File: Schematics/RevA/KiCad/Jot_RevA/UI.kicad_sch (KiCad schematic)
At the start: 0 parts

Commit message: UI sheet: SW1 side button on BTN; buzzer BZ1 on +BATT with Q1 AO3400A low-side switch, R12 gate pull-down, D4 flyback, BUZZER_PWM
Co-Authored-By: Claude Opus 5.5 <noreply@anthropic.com>
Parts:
- added BZ1: MLT-5020, symbol Device:Buzzer
- added D4: 1N4148W, symbol Device:D
- added Q1: AO3400A, Package_TO_SOT_SMD:SOT-23, symbol Transistor_FET:AO3400A
- added R12: 100k, symbol Device:R
- added SW1: SW_Push, symbol Switch:SW_Push
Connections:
- new net: BZ1.2 (-), D4.2 (A), Q1.3 (D)
- new net +BATT: BZ1.1 (+), D4.1 (K)
- new net BTN: SW1.1
- new net BUZZER_PWM: Q1.1 (G), R12.1
- new net GND: Q1.2 (S), R12.2, SW1.2

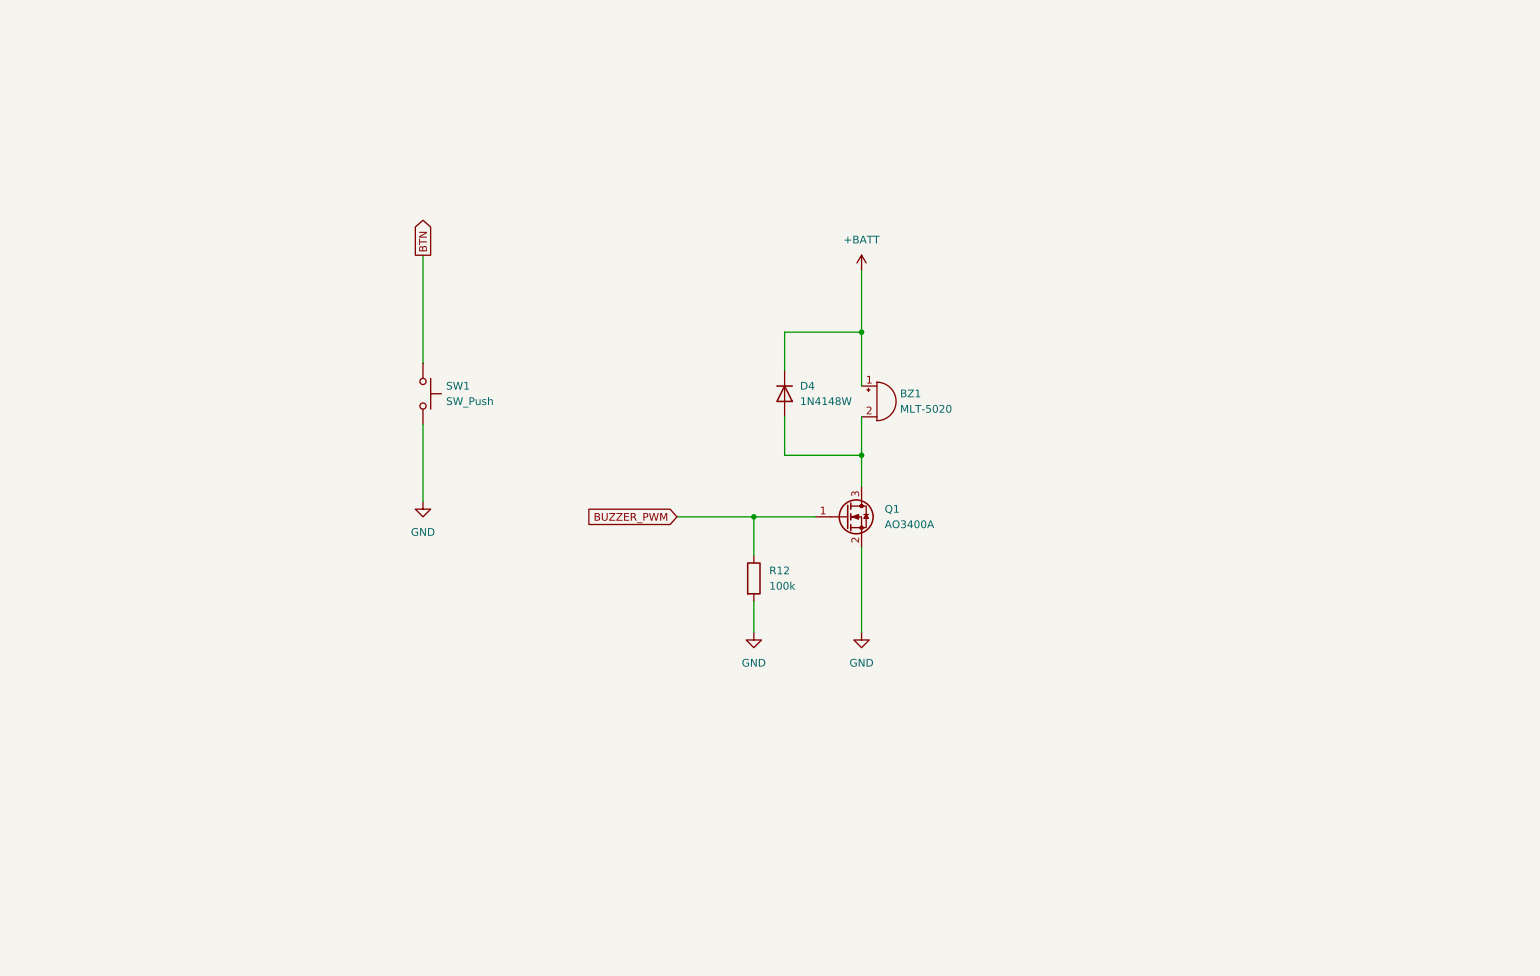
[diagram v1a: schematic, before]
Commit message: UI sheet: RGB LED D2 (common anode on +BATT) with R8 1k / R9 560 / R10 560 to Q3/Q4/Q5 low-side switches, R15-R17 gate pull-downs, LED_R/G/B labels
Co-Authored-By: Claude Opus 5.5 <noreply@anthropic.com>
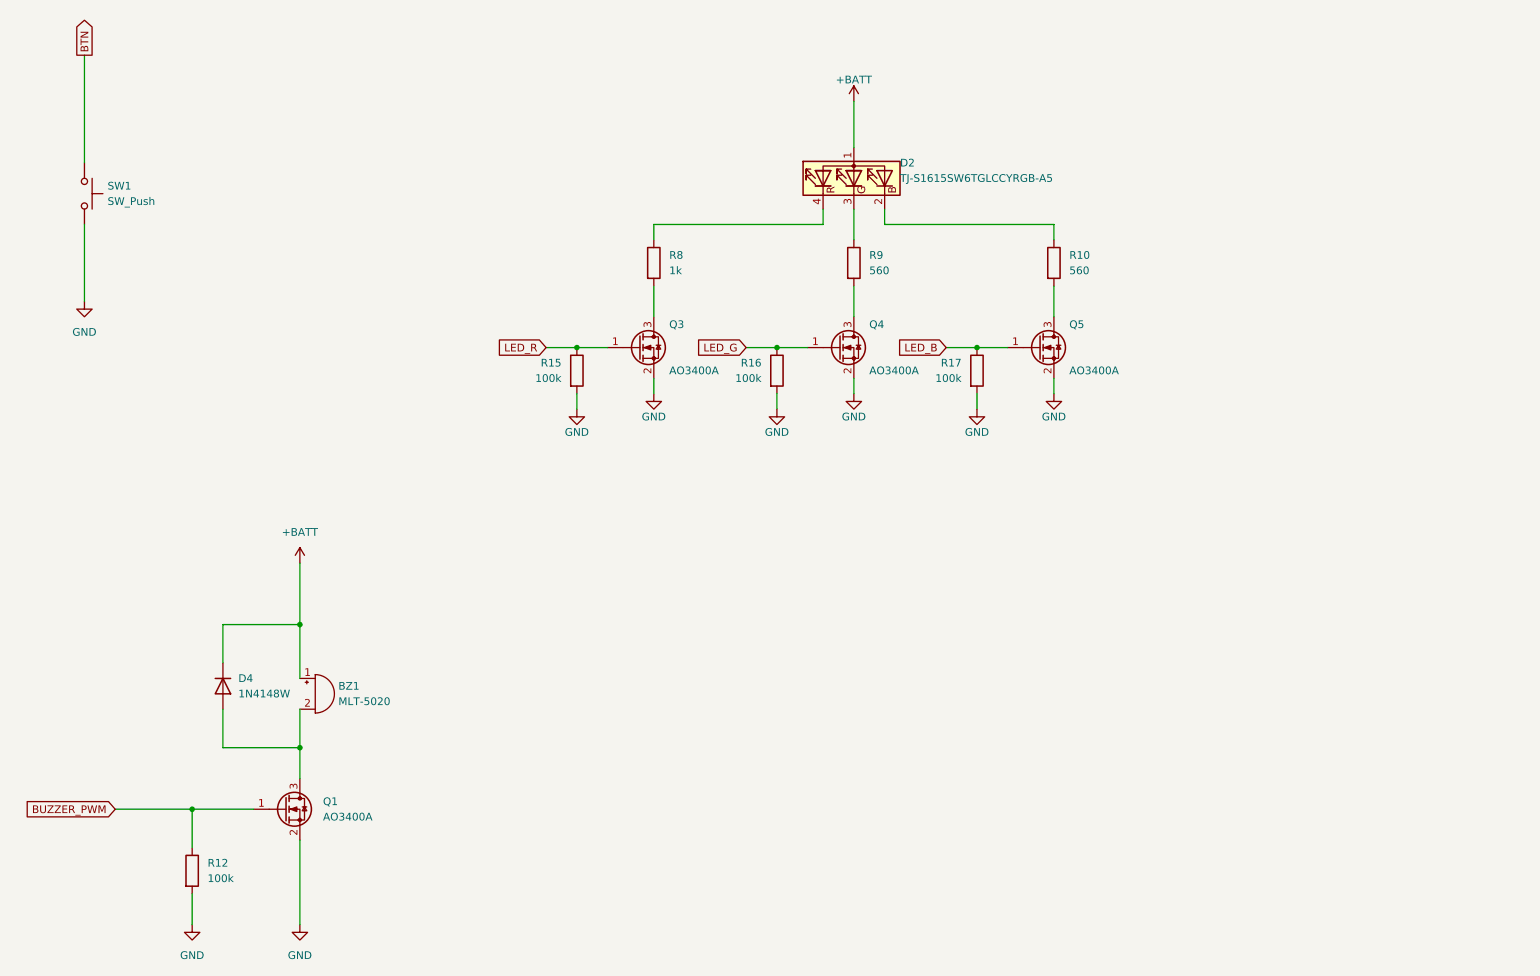
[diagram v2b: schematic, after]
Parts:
- added D2: TJ-S1615SW6TGLCCYRGB-A5, symbol Jot:TJ-S1615SW6TGLCCYRGB-A5
- added Q3, Q4, Q5: AO3400A, Package_TO_SOT_SMD:SOT-23, symbol Transistor_FET:AO3400A
- added R10, R9: 560, symbol Device:R
- added R15, R16, R17: 100k, symbol Device:R
- added R8: 1k, symbol Device:R
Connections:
- net +BATT: now also D2.1 (A)
- net GND: now also Q3.2 (S), Q4.2 (S), Q5.2 (S), R15.2, R16.2, R17.2
- new net: D2.2 (BK), R10.1
- new net: Q5.3 (D), R10.2
- new net: D2.3 (GK), R9.1
- new net: D2.4 (RK), R8.1
- new net: Q3.3 (D), R8.2
- new net: Q4.3 (D), R9.2
- new net LED_B: Q5.1 (G), R17.1
- new net LED_G: Q4.1 (G), R16.1
- new net LED_R: Q3.1 (G), R15.1
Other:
- moved on the sheet: BZ1, D4, Q1, R12, SW1

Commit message: Debug sheet: TP3-TP9 test pads for SWDIO, SWDCLK, nRESET, +3V3, GND, UART_TX, UART_RX; UI sheet re-laid out (nets unchanged)
Co-Authored-By: Claude Opus 5.5 <noreply@anthropic.com>
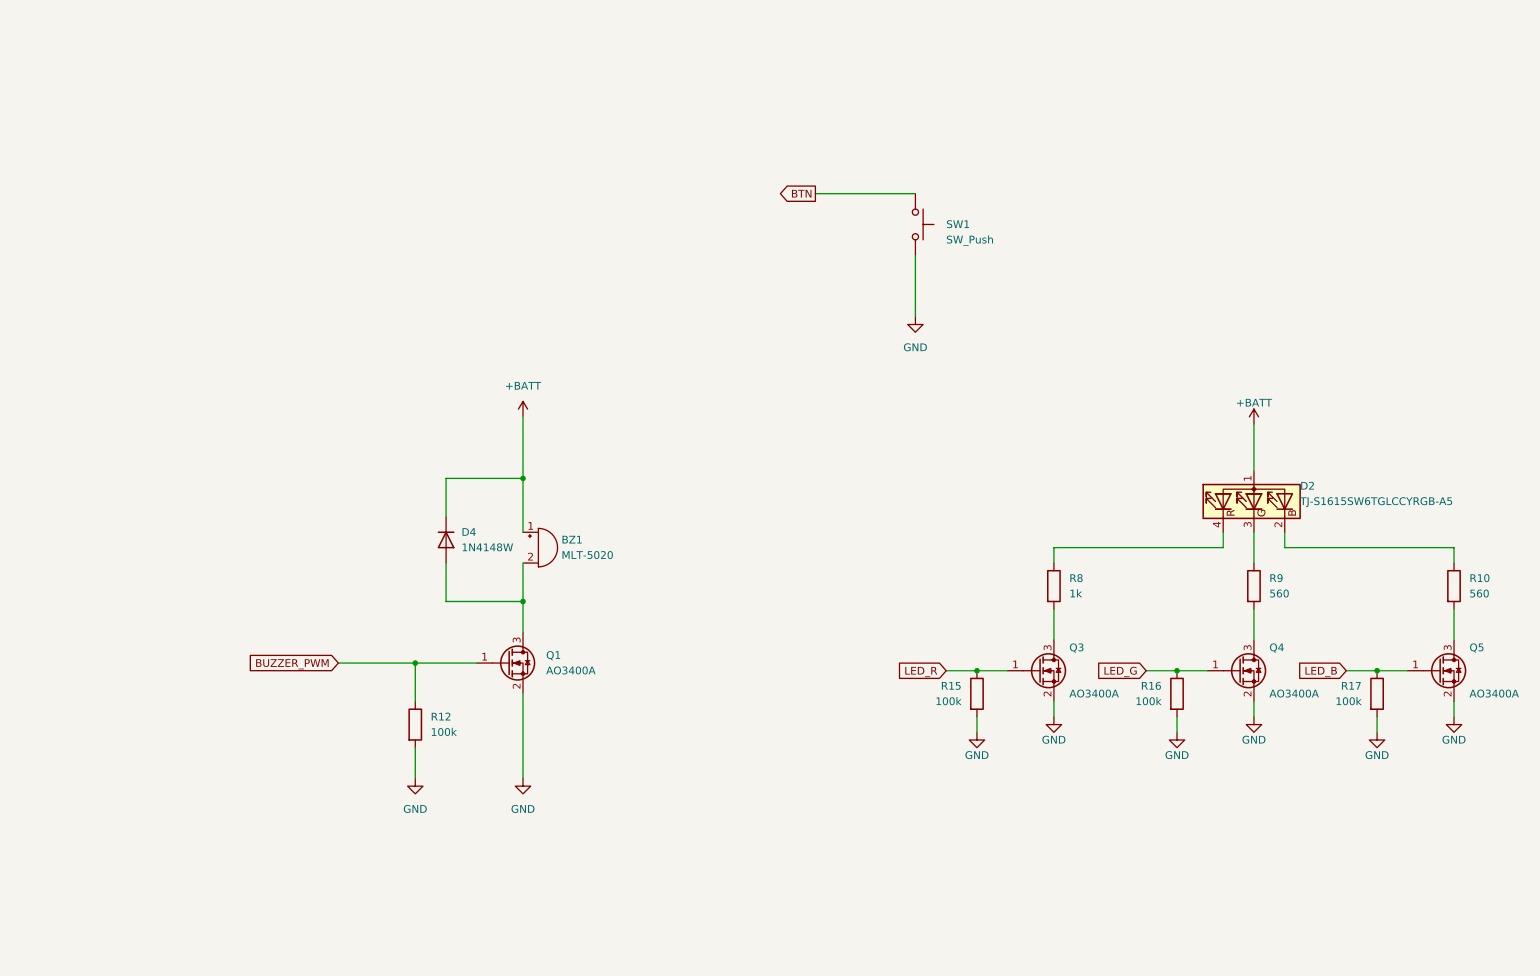
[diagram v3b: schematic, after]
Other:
- moved on the sheet: BZ1, D2, D4, Q1, Q3, Q4, Q5, R10, R12, R15, R16, R17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

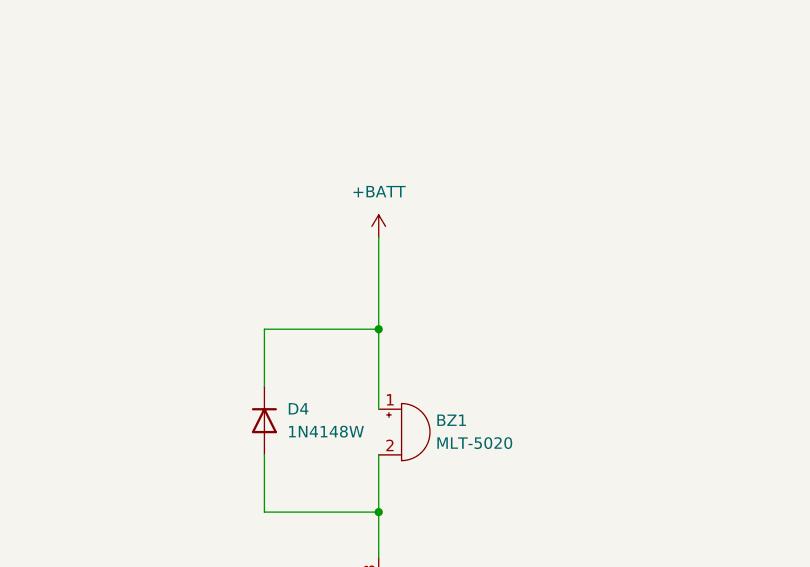
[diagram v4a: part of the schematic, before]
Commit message: Schematic review fixes: R18 100k flash /CS pull-up, R19 10R buzzer series resistor, T3902 DATA pin tri-state (ERC clean); BOM quantities and pin list updated
Co-Authored-By: Claude Opus 5.5 <noreply@anthropic.com>
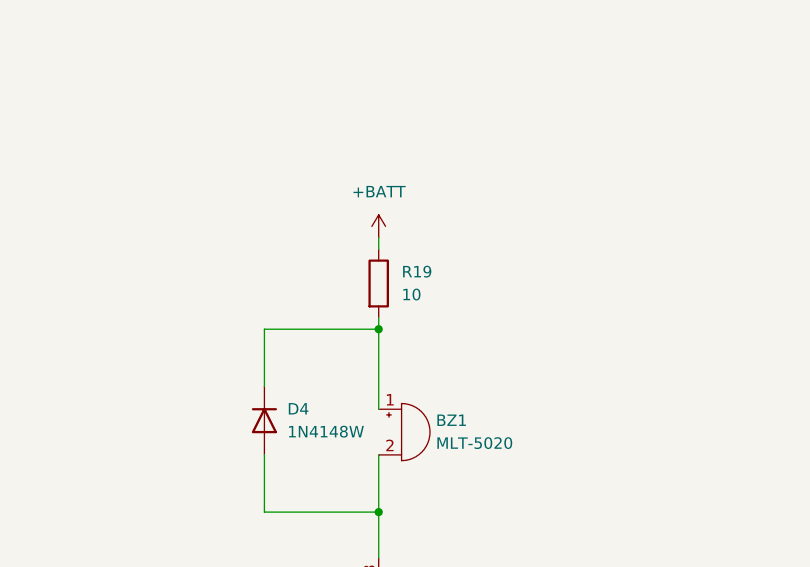
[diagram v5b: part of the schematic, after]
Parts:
- added R19: 10, symbol Device:R
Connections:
- net +BATT: now also R19.1; no longer BZ1.1 (+), D4.1 (K)
- new net: BZ1.1 (+), D4.1 (K), R19.2
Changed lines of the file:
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@@
-	(wire
-		(pts
-			(xy 97.79 85.09) (xy 97.79 95.25)
-		)
-		(stroke
-			(width 0)
-			(type default)
-		)
-	)
 	(wire
 		(pts
@@
 		)
 	)
+	(symbol
+		(lib_id "Device:R")
+		(at 97.79 90.17 0)
+		(unit 1)
+		(body_style 1)
+		(exclude_from_sim no)
+		(in_bom yes)
+		(on_board yes)
+		(in_pos_files yes)
+		(dnp no)
+		(property "Reference" "R19"
+			(at 100.33 88.9 0)
+			(show_name no)
+			(do_not_autoplace no)
+			(effects
+				(font
+					(size 1.27 1.27)
+				)
+				(justify left)
+			)
+		)
+		(property "Value" "10"
+			(at 100.33 91.44 0)
+			(show_name no)
+			(do_not_autoplace no)
+			(effects
+				(font
+					(size 1.27 1.27)
+				)
+				(justify left)
+			)
+		)
+		(property "Footprint" ""
+			(at 97.79 90.17 0)
+			(show_name no)
+			(do_not_autoplace no)
+			(hide yes)
+			(effects
+				(font
+					(size 1.27 1.27)
+				)
+			)
+		)
+		(property "Datasheet" ""
+			(at 97.79 90.17 0)
+			(show_name no)
+			(do_not_autoplace no)
+			(hide yes)
+			(effects
+				(font
+					(size 1.27 1.27)
+				)
+			)
+		)
+		(property "Description" "Resistor"
+			(at 97.79 90.17 0)
+			(show_name no)
+			(do_not_autoplace no)
+			(hide yes)
+			(effects
+				(font
+					(size 1.27 1.27)
+				)
+			)
+		)
+		(pin "1"
+		)
+		(pin "2"
+		)
+		(instances
+			(project "Jot_RevA"
+				(path "/61747270-9f90-47b6-9c50-5ea1f41f259a/32fe5d00-0189-4157-8ea0-b1e59c92ae9f"
+					(reference "R19")
+					(unit 1)
+				)
+			)
+		)
+	)
+	(wire
+		(pts
+			(xy 97.79 85.09) (xy 97.79 86.36)
+		)
+		(stroke
+			(width 0)
+			(type default)
+		)
+	)
+	(wire
+		(pts
+			(xy 97.79 93.98) (xy 97.79 95.25)
+		)
+		(stroke
+			(width 0)
+			(type default)
+		)
+	)

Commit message: Footprints: all resistors (0402, R19 1206) and capacitors (0402, 10 uF 0603) assigned to match the BOM
Co-Authored-By: Claude Opus 5.5 <noreply@anthropic.com>
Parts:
- R10, R12, R15, R16, R17, R8, R9: footprint (none) -> Resistor_SMD:R_0402_1005Metric
- R19: footprint (none) -> Resistor_SMD:R_1206_3216Metric
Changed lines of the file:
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@@
+	(wire
+		(pts
+			(xy 97.79 85.09) (xy 97.79 86.36)
+		)
+		(stroke
+			(width 0)
+			(type default)
+		)
+	)
 	(wire
 		(pts
@@
 		(pts
 			(xy 238.76 127) (xy 233.68 127)
+		)
+		(stroke
+			(width 0)
+			(type default)
+		)
+	)
+	(wire
+		(pts
+			(xy 97.79 93.98) (xy 97.79 95.25)
 		)
 		(stroke
@@
 			)
 		)
-		(property "Footprint" ""
+		(property "Footprint" "Resistor_SMD:R_0402_1005Metric"
 			(at 238.76 130.81 0)
 			(hide yes)
@@
 			)
 		)
-		(property "Footprint" ""
+		(property "Footprint" "Resistor_SMD:R_0402_1005Metric"
 			(at 251.46 113.03 0)
 			(hide yes)
@@
 			)
 		)
-		(property "Footprint" ""
+		(property "Footprint" "Resistor_SMD:R_0402_1005Metric"
 			(at 205.74 130.81 0)
 			(hide yes)
@@
 			)
 		)
-		(property "Footprint" ""
+		(property "Footprint" "Resistor_SMD:R_0402_1005Metric"
 			(at 172.72 130.81 0)
 			(hide yes)
@@
 	)
 	(symbol
+		(lib_id "Device:R")
+		(at 97.79 90.17 0)
+		(unit 1)
+		(body_style 1)
+		(exclude_from_sim no)
+		(in_bom yes)
+		(on_board yes)
+		(in_pos_files yes)
+		(dnp no)
+		(property "Reference" "R19"
+			(at 100.33 88.9 0)
+			(show_name no)
+			(do_not_autoplace no)
+			(effects
+				(font
+					(size 1.27 1.27)
+				)
+				(justify left)
+			)
+		)
+		(property "Value" "10"
+			(at 100.33 91.44 0)
+			(show_name no)
+			(do_not_autoplace no)
+			(effects
+				(font
+					(size 1.27 1.27)
+				)
+				(justify left)
+			)
+		)
+		(property "Footprint" "Resistor_SMD:R_1206_3216Metric"
+			(at 97.79 90.17 0)
+			(hide yes)
+			(show_name no)
+			(do_not_autoplace no)
+			(effects
+				(font
+					(size 1.27 1.27)
+				)
+			)
+		)
+		(property "Datasheet" ""
+			(at 97.79 90.17 0)
+			(hide yes)
+			(show_name no)
+			(do_not_autoplace no)
+			(effects
+				(font
+					(size 1.27 1.27)
+				)
+			)
+		)
+		(property "Description" "Resistor"
+			(at 97.79 90.17 0)
+			(hide yes)
+			(show_name no)
+			(do_not_autoplace no)
+			(effects
+				(font
+					(size 1.27 1.27)
+				)
+			)
+		)
+		(pin "1"
+		)
+		(pin "2"
+		)
+		(instances
+			(project "Jot_RevA"
+				(path "/61747270-9f90-47b6-9c50-5ea1f41f259a/32fe5d00-0189-4157-8ea0-b1e59c92ae9f"
+					(reference "R19")
+					(unit 1)
+				)
+			)
+		)
+	)
+	(symbol
 		(lib_id "power:GND")
 		(at 97.79 144.78 0)
@@
 			)
 		)
-		(property "Footprint" ""
+		(property "Footprint" "Resistor_SMD:R_0402_1005Metric"
 			(at 185.42 113.03 0)
 			(hide yes)
@@
 			)
 		)
-		(property "Footprint" ""
+		(property "Footprint" "Resistor_SMD:R_0402_1005Metric"
 			(at 78.232 135.89 90)
 			(hide yes)
@@
 			)
 		)
-		(property "Footprint" ""
+		(property "Footprint" "Resistor_SMD:R_0402_1005Metric"
 			(at 218.44 113.03 0)
 			(hide yes)
@@
 		)
 	)
-	(symbol
-		(lib_id "Device:R")
-		(at 97.79 90.17 0)
-		(unit 1)
-		(body_style 1)
-		(exclude_from_sim no)
-		(in_bom yes)
-		(on_board yes)
-		(in_pos_files yes)
-		(dnp no)
-		(property "Reference" "R19"
-			(at 100.33 88.9 0)
-			(show_name no)
-			(do_not_autoplace no)
-			(effects
-				(font
-					(size 1.27 1.27)
-				)
-				(justify left)
-			)
-		)
-		(property "Value" "10"
-			(at 100.33 91.44 0)
-			(show_name no)
-			(do_not_autoplace no)
-			(effects
-				(font
-					(size 1.27 1.27)
-				)
-				(justify left)
-			)
-		)
-		(property "Footprint" ""
-			(at 97.79 90.17 0)
-			(show_name no)
-			(do_not_autoplace no)
-			(hide yes)
-			(effects
-				(font
-					(size 1.27 1.27)
-				)
-			)
-		)
-		(property "Datasheet" ""
-			(at 97.79 90.17 0)
-			(show_name no)
-			(do_not_autoplace no)
-			(hide yes)
-			(effects
-				(font
-					(size 1.27 1.27)
-				)
-			)
-		)
-		(property "Description" "Resistor"
-			(at 97.79 90.17 0)
-			(show_name no)
-			(do_not_autoplace no)
-			(hide yes)
-			(effects
-				(font
-					(size 1.27 1.27)
-				)
-			)
-		)
-		(pin "1"
-		)
-		(pin "2"
-		)
-		(instances
-			(project "Jot_RevA"
-				(path "/61747270-9f90-47b6-9c50-5ea1f41f259a/32fe5d00-0189-4157-8ea0-b1e59c92ae9f"
-					(reference "R19")
-					(unit 1)
-				)
-			)
-		)
-	)
-	(wire
-		(pts
-			(xy 97.79 85.09) (xy 97.79 86.36)
-		)
-		(stroke
-			(width 0)
-			(type default)
-		)
-	)
-	(wire
-		(pts
-			(xy 97.79 93.98) (xy 97.79 95.25)
-		)
-		(stroke
-			(width 0)
-			(type default)
-		)
-	)

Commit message: Footprints: D1 LED 0603, D4 SOD-123, Y1 3215 crystal
Co-Authored-By: Claude Opus 5.5 <noreply@anthropic.com>
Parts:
- D4: footprint (none) -> Diode_SMD:D_SOD-123
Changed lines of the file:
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@@
 			)
 		)
-		(property "Footprint" ""
+		(property "Footprint" "Diode_SMD:D_SOD-123"
 			(at 85.09 105.41 0)
 			(hide yes)

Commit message: Footprints: D2 RGB LED (new project library Jot.pretty, built from TOGIALED pad layout), J1 HRO TYPE-C-31-M-12, J2 JST S2B-PH-SM4-TB; project fp-lib-table
Co-Authored-By: Claude Opus 5.5 <noreply@anthropic.com>
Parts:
- D2: footprint (none) -> Jot:LED_RGB_TOGIALED_1615_1.6x1.5mm
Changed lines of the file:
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@@
 			)
 		)
-		(property "Footprint" ""
+		(property "Footprint" "Jot:LED_RGB_TOGIALED_1615_1.6x1.5mm"
 			(at 218.44 99.06 0)
 			(hide yes)
